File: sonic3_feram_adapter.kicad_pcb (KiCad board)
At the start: 2 copper layers, 17.8 x 30.5 mm, 6 parts, among them IC1 FM16W08-SG, P1 CONN_02X12

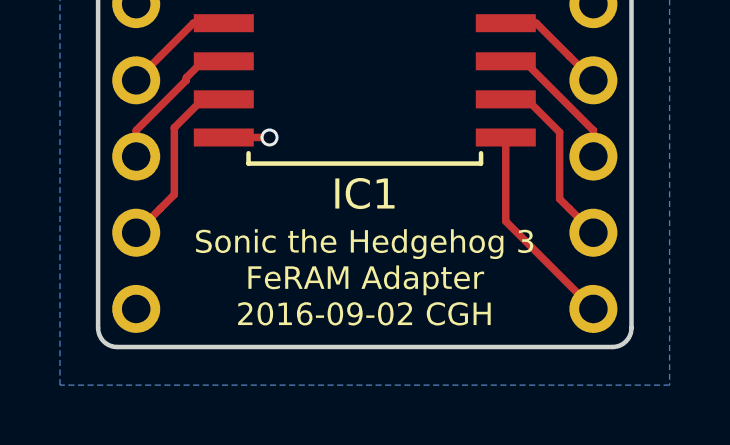
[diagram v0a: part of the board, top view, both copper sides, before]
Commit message: Updated date on silkscreen
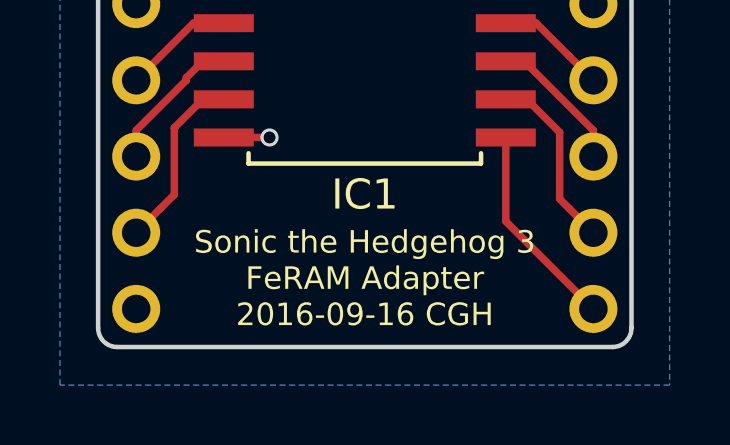
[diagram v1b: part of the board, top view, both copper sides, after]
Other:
- board text added: "Sonic the Hedgehog 3 FeRAM Adapter 2016-09-16 CGH"
- board text removed: "Sonic the Hedgehog 3 FeRAM Adapter 2016-09-02 CGH"
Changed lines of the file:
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@@
     (effects (font (size 0.75 0.75) (thickness 0.15)) (justify left mirror))
   )
-  (gr_text "Sonic the Hedgehog 3\nFeRAM Adapter\n2016-09-02 CGH" (at 76.2 89.154) (layer F.SilkS)
+  (gr_text "Sonic the Hedgehog 3\nFeRAM Adapter\n2016-09-16 CGH" (at 76.2 89.154) (layer F.SilkS)
     (effects (font (size 0.75 0.75) (thickness 0.15)))
   )
